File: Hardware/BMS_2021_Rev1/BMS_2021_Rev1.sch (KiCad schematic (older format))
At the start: 3 parts

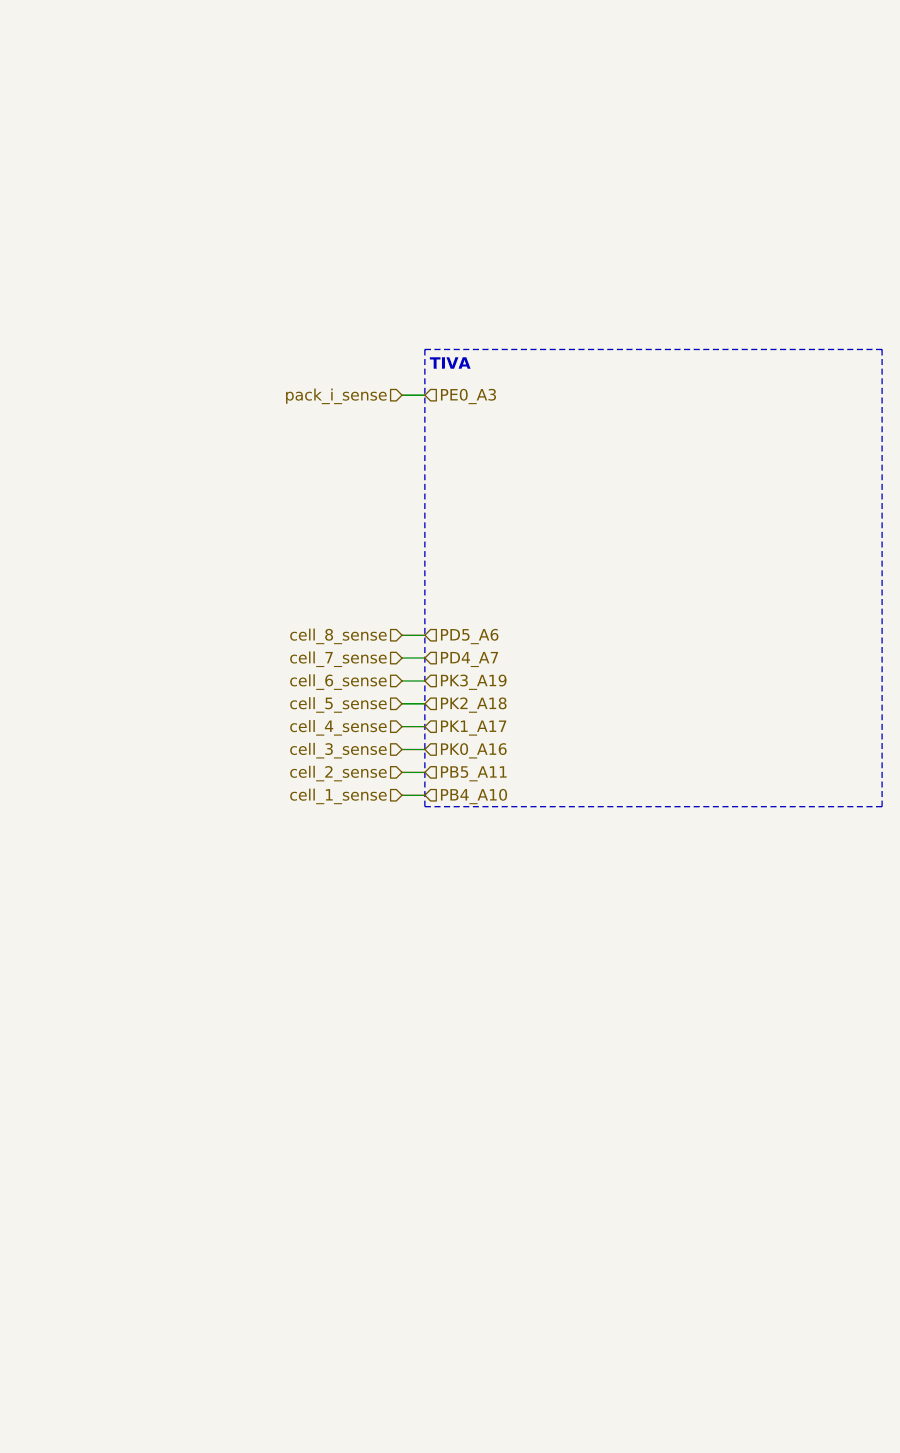
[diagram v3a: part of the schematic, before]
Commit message: changed layout
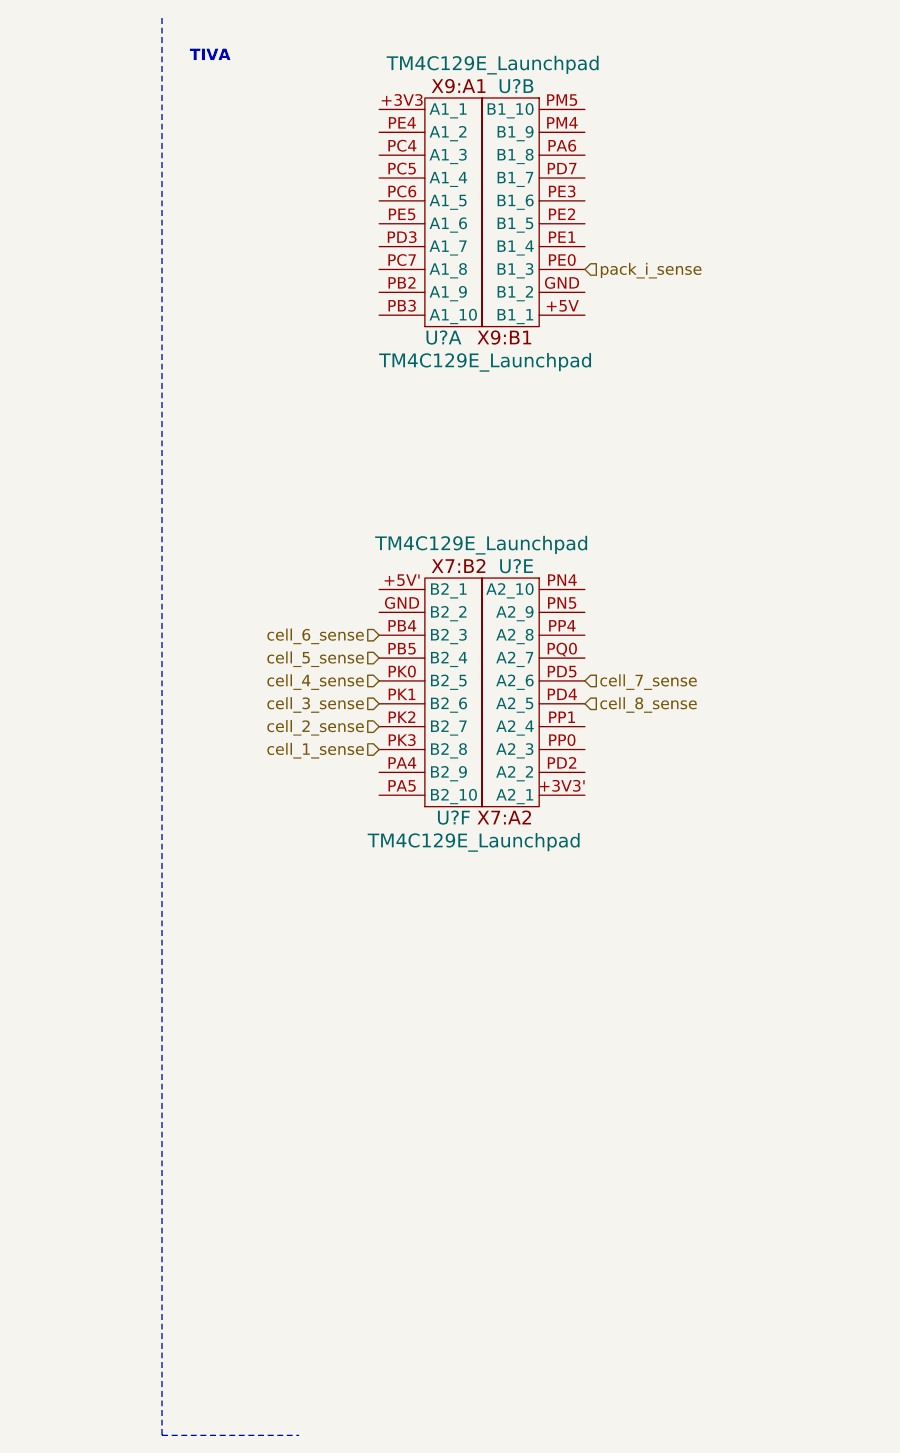
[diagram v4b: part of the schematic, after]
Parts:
- added U? (x4): TM4C129E_Launchpad, symbol MRDT_Shields:TM4C129E_Launchpad
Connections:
- new net cell_1_sense: U?.PK3 (B2_8)
- new net cell_2_sense: U?.PK2 (B2_7)
- new net cell_3_sense: U?.PK1 (B2_6)
- new net cell_4_sense: U?.PK0 (B2_5)
- new net cell_5_sense: U?.PB5 (B2_4)
- new net cell_6_sense: U?.PB4 (B2_3)
- new net cell_7_sense: U?.PD5 (A2_6)
- new net cell_8_sense: U?.PD4 (A2_5)
- new net pack_i_sense: U?.PE0 (B1_3)
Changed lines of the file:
@@
 Text HLabel 1050 2250 2    50   Input ~ 0
 GND
-Wire Notes Line
-	7800 1950 7800 3950
-Wire Notes Line
-	7800 3950 9800 3950
-Wire Notes Line
-	9800 3950 9800 1950
-Wire Notes Line
-	9800 1950 7800 1950
-Text Notes 8000 2050 2    50   ~ 10
+Text Notes 6950 700  2    50   ~ 10
 TIVA
-Text HLabel 7700 3900 0    50   Input ~ 0
+Text HLabel 7600 3700 0    50   Input ~ 0
 cell_1_sense
-Text HLabel 7700 3200 0    50   Input ~ 0
+Text HLabel 8500 3500 2    50   Input ~ 0
 cell_8_sense
-Text HLabel 7700 3300 0    50   Input ~ 0
+Text HLabel 8500 3400 2    50   Input ~ 0
 cell_7_sense
-Text HLabel 7700 3400 0    50   Input ~ 0
+Text HLabel 7600 3200 0    50   Input ~ 0
 cell_6_sense
-Text HLabel 7700 3500 0    50   Input ~ 0
+Text HLabel 7600 3300 0    50   Input ~ 0
 cell_5_sense
-Text HLabel 7700 3600 0    50   Input ~ 0
+Text HLabel 7600 3400 0    50   Input ~ 0
 cell_4_sense
-Text HLabel 7700 3700 0    50   Input ~ 0
+Text HLabel 7600 3500 0    50   Input ~ 0
 cell_3_sense
-Text HLabel 7700 3800 0    50   Input ~ 0
+Text HLabel 7600 3600 0    50   Input ~ 0
 cell_2_sense
-Text HLabel 7800 3900 2    50   Input ~ 0
-PB4_A10
-Text HLabel 7800 3800 2    50   Input ~ 0
-PB5_A11
-Text HLabel 7800 3700 2    50   Input ~ 0
-PK0_A16
-Text HLabel 7800 3600 2    50   Input ~ 0
-PK1_A17
-Text HLabel 7800 3500 2    50   Input ~ 0
-PK2_A18
-Text HLabel 7800 3400 2    50   Input ~ 0
-PK3_A19
-Text HLabel 7800 3300 2    50   Input ~ 0
-PD4_A7
-Text HLabel 7800 3200 2    50   Input ~ 0
-PD5_A6
-Wire Wire Line
-	7700 3200 7800 3200
-Wire Wire Line
-	7700 3300 7800 3300
-Wire Wire Line
-	7700 3400 7800 3400
-Wire Wire Line
-	7700 3500 7800 3500
-Wire Wire Line
-	7700 3600 7800 3600
-Wire Wire Line
-	7700 3700 7800 3700
-Wire Wire Line
-	7700 3800 7800 3800
-Wire Wire Line
-	7700 3900 7800 3900
 Text HLabel 900  1250 0    50   Output ~ 0
 V_in
@@
 Text HLabel 3300 850  2    50   Output ~ 0
 pack_i_sense
-Text HLabel 7700 2150 0    50   Input ~ 0
+Text HLabel 8500 1600 2    50   Input ~ 0
 pack_i_sense
-Text HLabel 7800 2150 2    50   Input ~ 0
-PE0_A3
-Wire Wire Line
-	7700 2150 7800 2150
 $Sheet
 S 2550 1350 750  300
@@
 Text Notes 1100 6350 0    50   ~ 0
 ENTER RESISTOR VALUES\n
+$Comp
+L MRDT_Shields:TM4C129E_Launchpad U?
+U 6 1 5F7FD340
+P 7800 3950
+F 0 "U?" H 7850 3900 60  0000 L CNN
+F 1 "TM4C129E_Launchpad" H 7550 3800 60  0000 L CNN
+F 2 "" H 7800 3950 60  0001 C CNN
+F 3 "" H 7800 3950 60  0001 C CNN
+	6    7800 3950
+	1    0    0    -1
+$EndComp
+$Comp
+L MRDT_Shields:TM4C129E_Launchpad U?
+U 5 1 5F805ECA
+P 8300 2950
+F 0 "U?" H 8400 2900 60  0000 C CNN
+F 1 "TM4C129E_Launchpad" H 8550 2800 60  0000 C CNN
+F 2 "" H 8300 2950 60  0001 C CNN
+F 3 "" H 8300 2950 60  0001 C CNN
+	5    8300 2950
+	-1   0    0    1
+$EndComp
+$Comp
+L MRDT_Shields:TM4C129E_Launchpad U?
+U 1 1 5F814779
+P 7800 1850
+F 0 "U?" H 7800 1800 60  0000 L CNN
+F 1 "TM4C129E_Launchpad" H 7600 1700 60  0000 L CNN
+F 2 "" H 7800 1850 60  0001 C CNN
+F 3 "" H 7800 1850 60  0001 C CNN
+	1    7800 1850
+	1    0    0    -1
+$EndComp
+$Comp
+L MRDT_Shields:TM4C129E_Launchpad U?
+U 2 1 5F81CC17
+P 8300 850
+F 0 "U?" H 8400 800 60  0000 C CNN
+F 1 "TM4C129E_Launchpad" H 8500 700 60  0000 C CNN
+F 2 "" H 8300 850 60  0001 C CNN
+F 3 "" H 8300 850 60  0001 C CNN
+	2    8300 850
+	-1   0    0    1
+$EndComp
+Wire Notes Line
+	6650 500  6650 6700
+Wire Notes Line
+	6650 6700 7250 6700
 $EndSCHEMATC

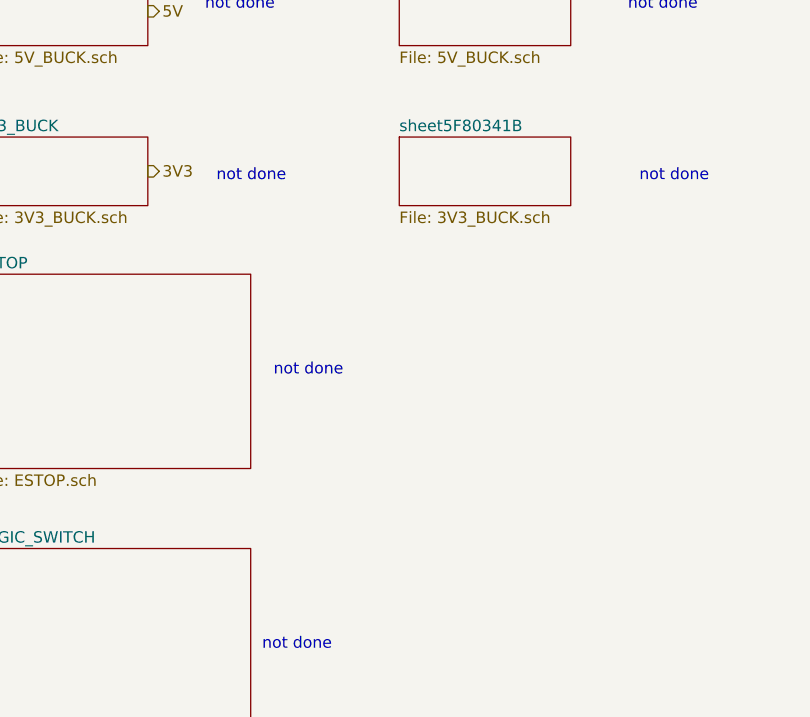
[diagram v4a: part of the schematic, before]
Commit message: cell filter mods, changing current sense circuit, 3v3/5v worked on
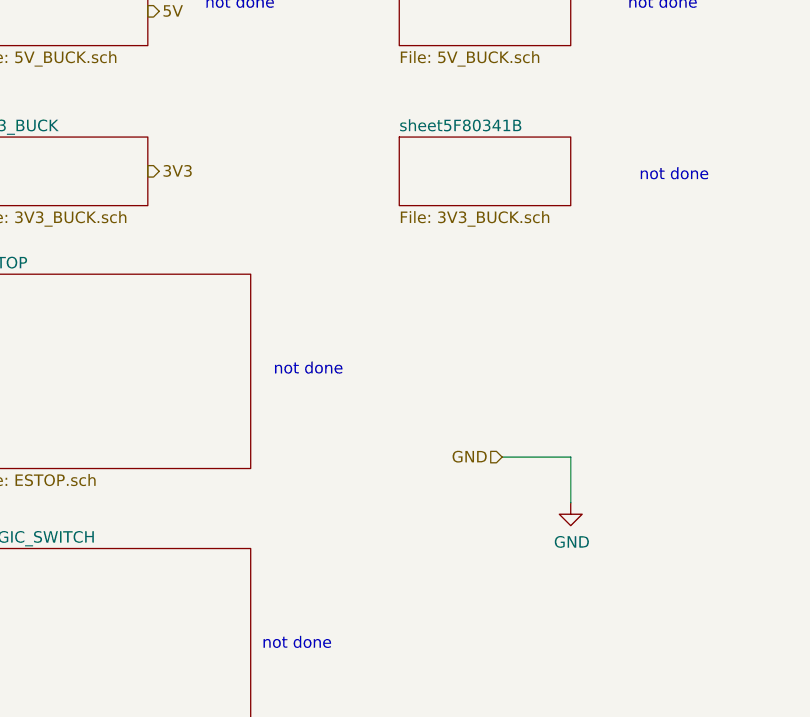
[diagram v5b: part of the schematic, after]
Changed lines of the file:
@@
 Text Notes 3550 1500 0    50   ~ 0
-not done
-Text Notes 3600 2250 0    50   ~ 0
 not done
 $Sheet
@@
 Wire Notes Line
 	6650 6700 7250 6700
+Text HLabel 4850 3450 0    50   Input ~ 0
+GND
+$Comp
+L power:GND #PWR?
+U 1 1 5F843586
+P 5150 3650
+F 0 "#PWR?" H 5150 3400 50  0001 C CNN
+F 1 "GND" H 5155 3477 50  0000 C CNN
+F 2 "" H 5150 3650 50  0001 C CNN
+F 3 "" H 5150 3650 50  0001 C CNN
+	1    5150 3650
+	1    0    0    -1
+$EndComp
+Wire Wire Line
+	4850 3450 5150 3450
+Wire Wire Line
+	5150 3450 5150 3650
 $EndSCHEMATC

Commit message: did some wiring n stuff
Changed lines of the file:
@@
 cell_2_sense
 Text HLabel 850  3500 0    50   Input ~ 0
-5V+
+PV
 Text HLabel 850  3600 0    50   Input ~ 0
 GND
@@
 not done
 $Sheet
-S 4400 1350 750  300
-U 5F803423
-F0 "sheet5F80341A" 50
-F1 "5V_BUCK.sch" 50
-$EndSheet
-$Sheet
 S 4400 2050 750  300
 U 5F80342B
@@
 Wire Wire Line
 	5150 3450 5150 3650
+$Sheet
+S 4400 1350 750  300
+U 5F803423
+F0 "TEMP_SENSE" 50
+F1 "TEMP_SENSE.sch" 50
+$EndSheet
 $EndSCHEMATC

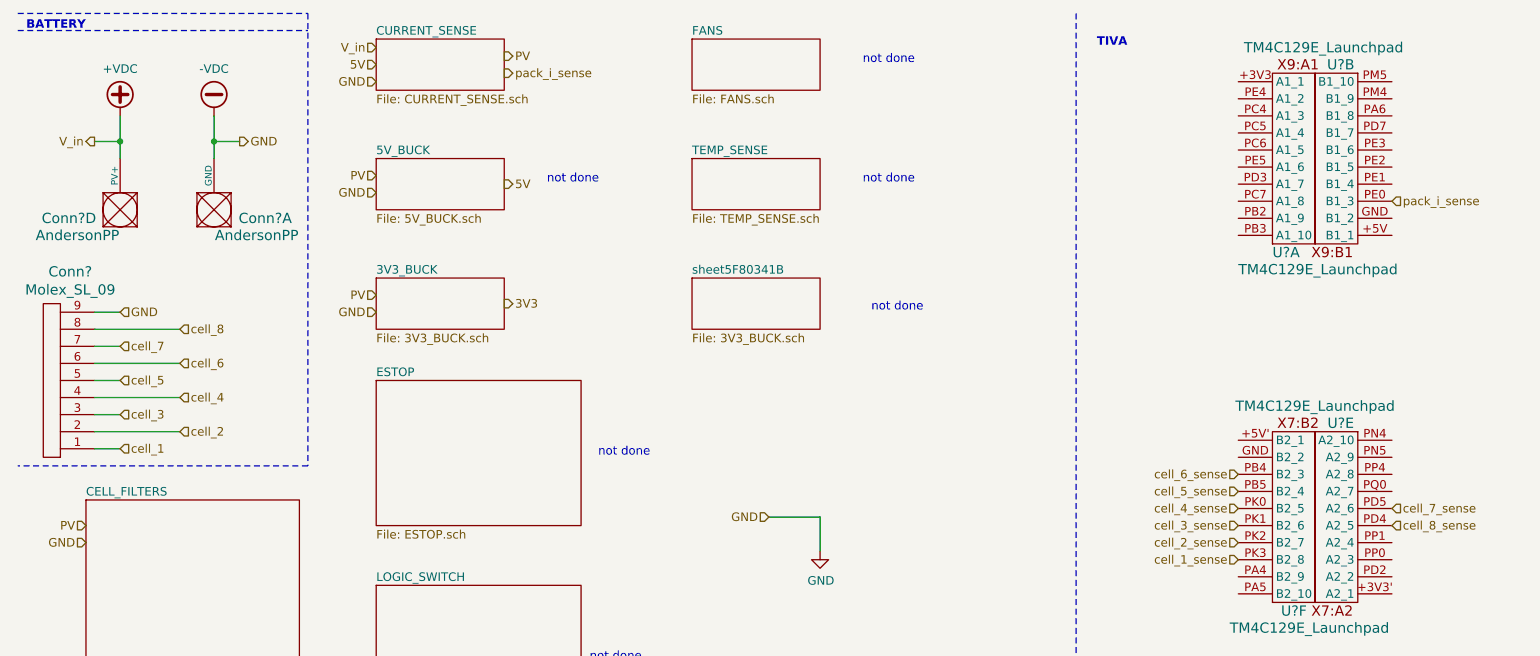
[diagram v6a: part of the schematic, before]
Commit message: buzzer started, 5v buck needs R values
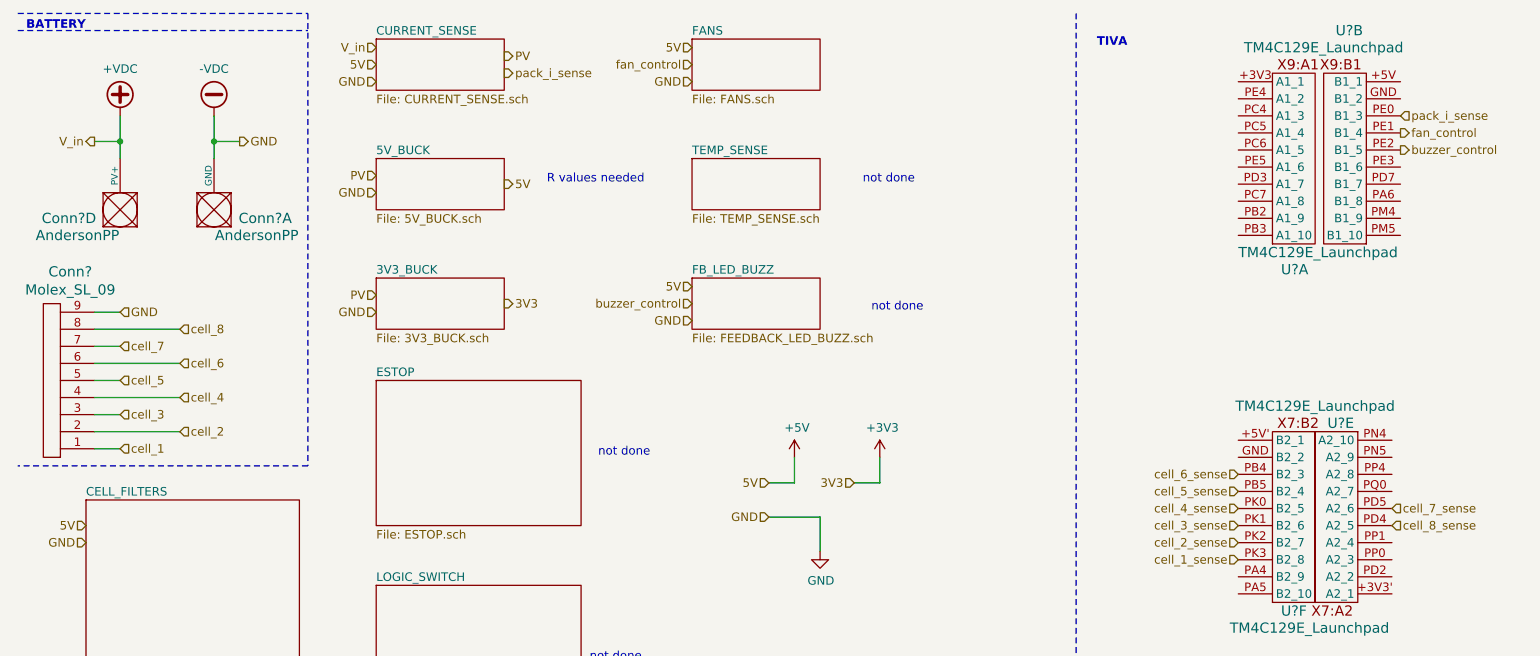
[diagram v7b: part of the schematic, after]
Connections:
- net fan_control: now reaches U?.PE1 (B1_4)
- net buzzer_control: now reaches U?.PE2 (B1_5)
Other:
- note added: "R values needed\n"
- moved on the sheet: U?B
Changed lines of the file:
@@
 cell_2_sense
 Text HLabel 850  3500 0    50   Input ~ 0
-PV
+5V
 Text HLabel 850  3600 0    50   Input ~ 0
 GND
@@
 Text HLabel 3300 850  2    50   Output ~ 0
 pack_i_sense
-Text HLabel 8500 1600 2    50   Input ~ 0
-pack_i_sense
 $Sheet
 S 2550 1350 750  300
@@
 $EndSheet
 Text Notes 3550 1500 0    50   ~ 0
-not done
+R values needed\n
 $Sheet
 S 2550 2650 1200 850
@@
 Text Notes 3800 4300 0    50   ~ 0
 not done
-$Sheet
-S 4400 2050 750  300
-U 5F80342B
-F0 "sheet5F80341B" 50
-F1 "3V3_BUCK.sch" 50
-$EndSheet
 Text Notes 5400 1500 0    50   ~ 0
 not done
@@
 Text HLabel 2550 800  0    50   Input ~ 0
 5V
-Text Notes 5400 800  0    50   ~ 0
-not done
-$Sheet
-S 4400 650  750  300
-U 5F80341F
-F0 "FANS" 50
-F1 "FANS.sch" 50
-$EndSheet
 Text Notes 1100 6350 0    50   ~ 0
 ENTER RESISTOR VALUES\n
@@
 U 1 1 5F814779
 P 7800 1850
-F 0 "U?" H 7800 1800 60  0000 L CNN
-F 1 "TM4C129E_Launchpad" H 7600 1700 60  0000 L CNN
+F 0 "U?" H 7850 1700 60  0000 L CNN
+F 1 "TM4C129E_Launchpad" H 7600 1800 60  0000 L CNN
 F 2 "" H 7800 1850 60  0001 C CNN
 F 3 "" H 7800 1850 60  0001 C CNN
 	1    7800 1850
 	1    0    0    -1
-$EndComp
-$Comp
-L MRDT_Shields:TM4C129E_Launchpad U?
-U 2 1 5F81CC17
-P 8300 850
-F 0 "U?" H 8400 800 60  0000 C CNN
-F 1 "TM4C129E_Launchpad" H 8500 700 60  0000 C CNN
-F 2 "" H 8300 850 60  0001 C CNN
-F 3 "" H 8300 850 60  0001 C CNN
-	2    8300 850
-	-1   0    0    1
 $EndComp
 Wire Notes Line
@@
 F1 "TEMP_SENSE.sch" 50
 $EndSheet
+Text HLabel 4400 700  0    50   Input ~ 0
+5V
+Text HLabel 4400 900  0    50   Input ~ 0
+GND
+Text HLabel 4400 800  0    50   Input ~ 0
+fan_control
+Text HLabel 4850 3250 0    50   Input ~ 0
+5V
+$Comp
+L power:+5V #PWR?
+U 1 1 5F86F576
+P 5000 3100
+F 0 "#PWR?" H 5000 2950 50  0001 C CNN
+F 1 "+5V" H 5015 3273 50  0000 C CNN
+F 2 "" H 5000 3100 50  0001 C CNN
+F 3 "" H 5000 3100 50  0001 C CNN
+	1    5000 3100
+	1    0    0    -1
+$EndComp
+Wire Wire Line
+	4850 3250 5000 3250
+Wire Wire Line
+	5000 3250 5000 3100
+Text HLabel 5350 3250 0    50   Input ~ 0
+3V3
+Wire Wire Line
+	5350 3250 5500 3250
+Wire Wire Line
+	5500 3250 5500 3100
+$Comp
+L power:+3V3 #PWR?
+U 1 1 5F870EB9
+P 5500 3100
+F 0 "#PWR?" H 5500 2950 50  0001 C CNN
+F 1 "+3V3" H 5515 3273 50  0000 C CNN
+F 2 "" H 5500 3100 50  0001 C CNN
+F 3 "" H 5500 3100 50  0001 C CNN
+	1    5500 3100
+	1    0    0    -1
+$EndComp
+Text HLabel 8550 1100 2    50   Input ~ 0
+pack_i_sense
+$Comp
+L MRDT_Shields:TM4C129E_Launchpad U?
+U 2 1 5F81CC17
+P 8350 1850
+F 0 "U?" H 8450 3100 60  0000 C CNN
+F 1 "TM4C129E_Launchpad" H 8600 3000 60  0000 C CNN
+F 2 "" H 8350 1850 60  0001 C CNN
+F 3 "" H 8350 1850 60  0001 C CNN
+	2    8350 1850
+	-1   0    0    -1
+$EndComp
+Text HLabel 8550 1200 2    50   Output ~ 0
+fan_control
+$Sheet
+S 4400 2050 750  300
+U 5F80342B
+F0 "FB_LED_BUZZ" 50
+F1 "FEEDBACK_LED_BUZZ.sch" 50
+$EndSheet
+$Sheet
+S 4400 650  750  300
+U 5F80341F
+F0 "FANS" 50
+F1 "FANS.sch" 50
+$EndSheet
+Text HLabel 4400 2200 0    50   Input ~ 0
+buzzer_control
+Text HLabel 8550 1300 2    50   Output ~ 0
+buzzer_control
+Text HLabel 4400 2100 0    50   Input ~ 0
+5V
+Text HLabel 4400 2300 0    50   Input ~ 0
+GND
 $EndSCHEMATC

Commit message: done (need to do LEDs)
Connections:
- net logic_power_sense: now reaches U?.PE3 (B1_6)
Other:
- note added: "put no connect on not used pin"
- note removed: "ENTER RESISTOR VALUES\n"
- note removed: "R values needed\n"
